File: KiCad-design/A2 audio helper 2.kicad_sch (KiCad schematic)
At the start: 34 parts, among them J1 PIN HEADER 1x2, J10 PIN HEADER 1x2, J11 PIN HEADER 1x3, J12 PIN HEADER 1x3, J13 PIN HEADER 1x3, J2 PIN HEADER 1x2, J3 PIN HEADER 1x2, J4 SJ1-3515N, J5 PIN HEADER 1x3, J6 PIN HEADER 1x3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

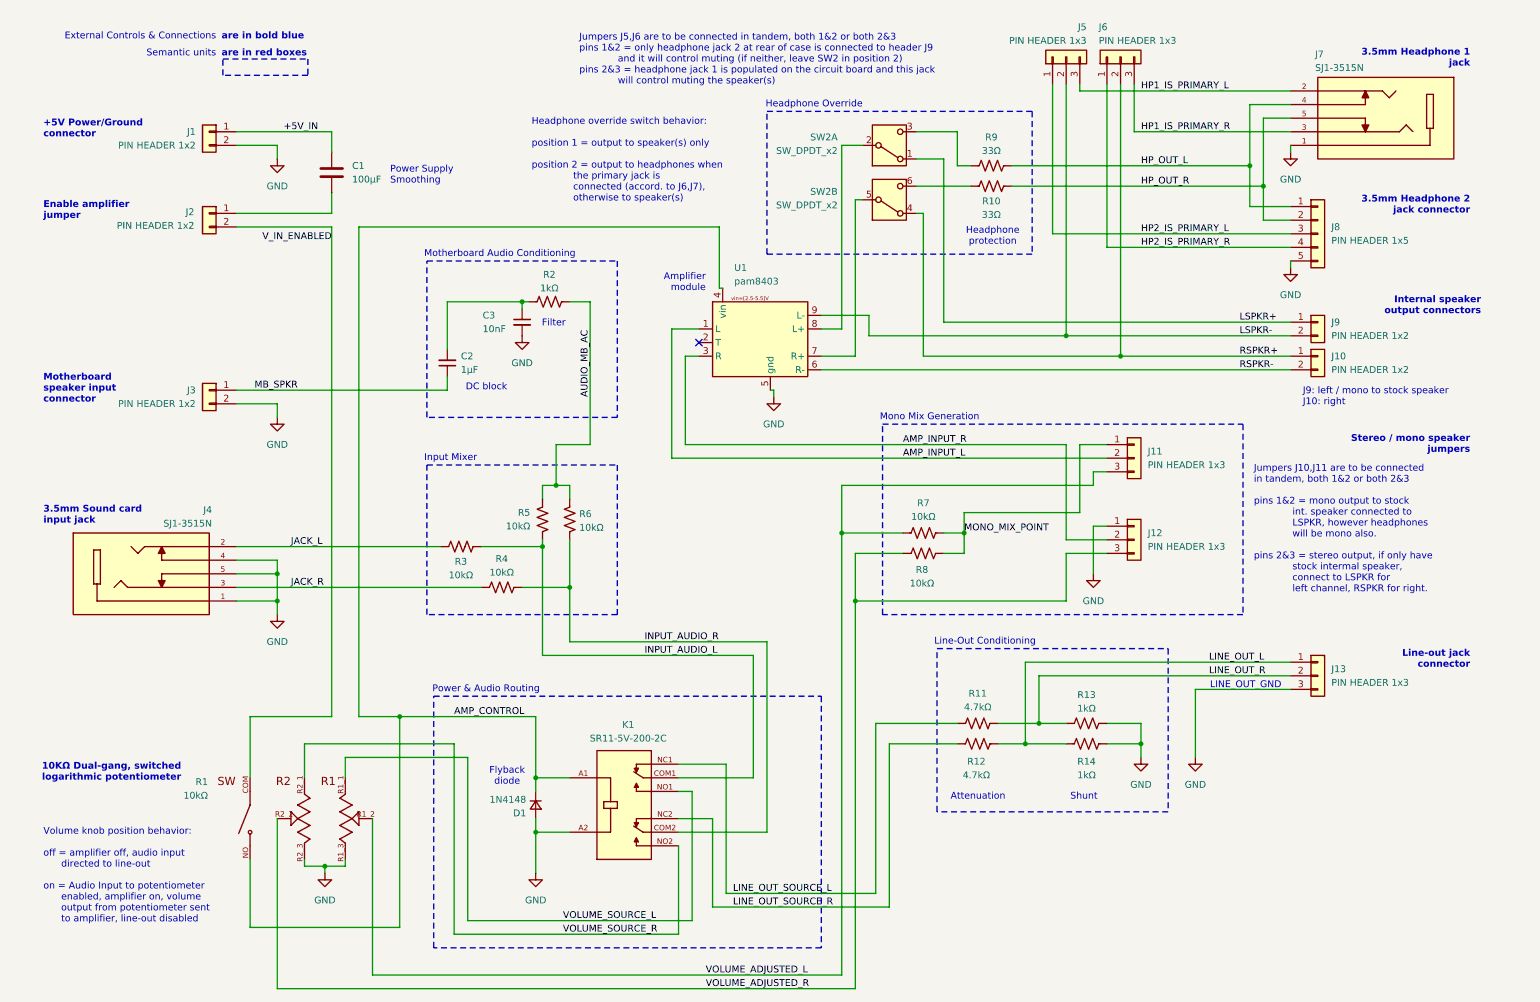
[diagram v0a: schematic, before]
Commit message: ribbon cbl to remote vol & headph board
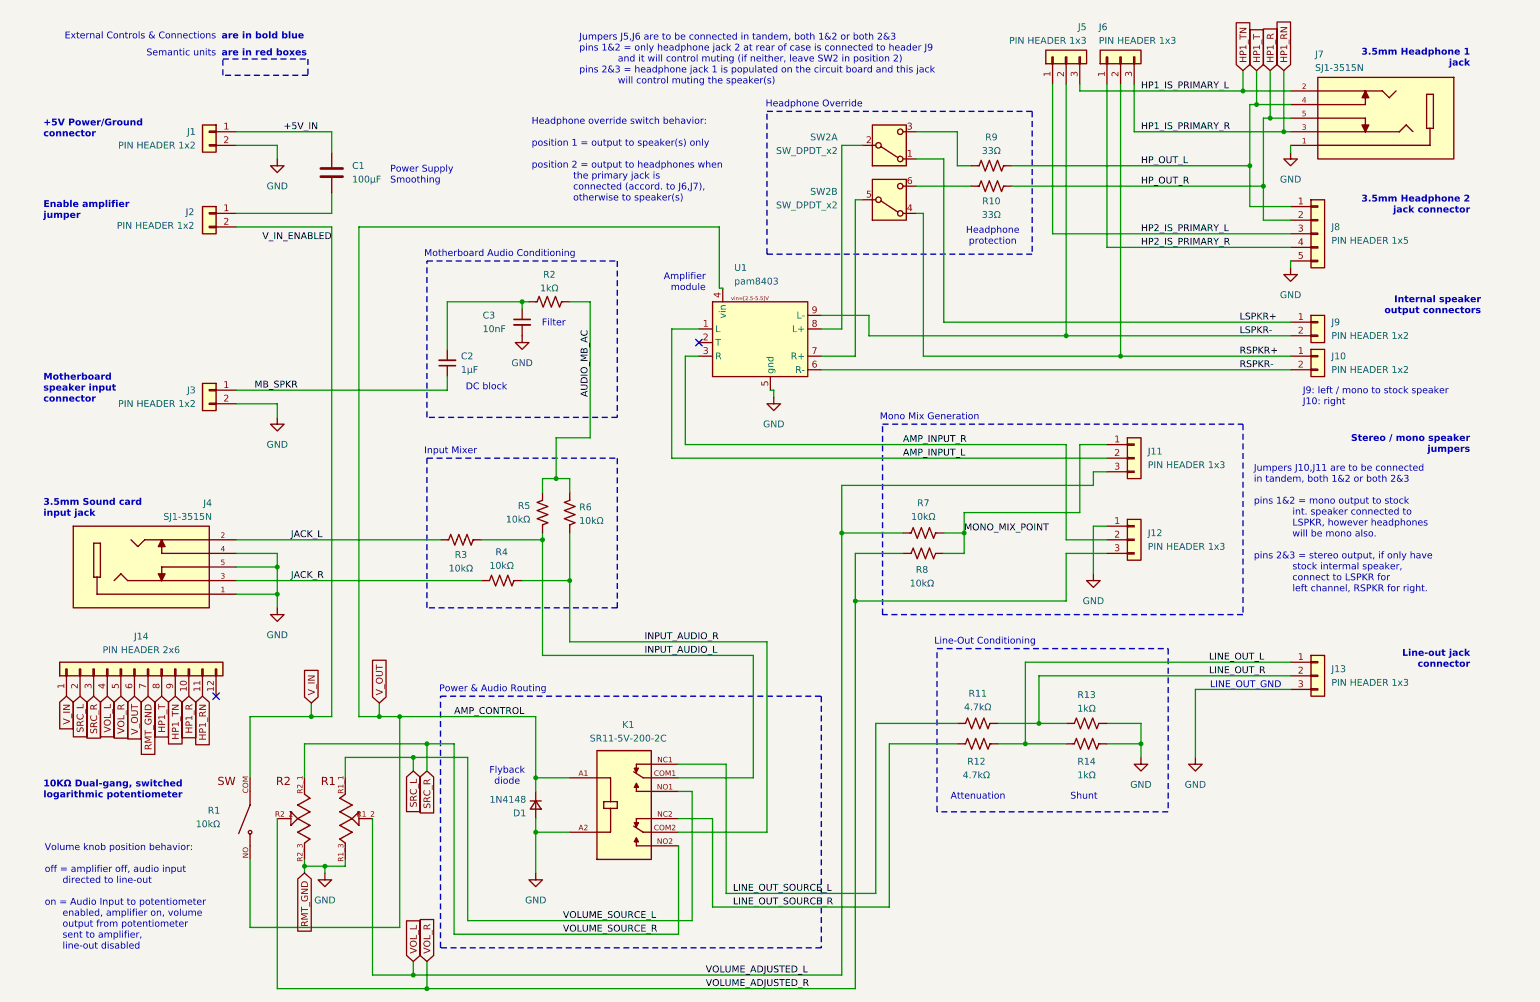
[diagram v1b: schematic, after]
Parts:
- added J14: PIN HEADER 2x6, Connector_PinSocket_2.00mm:PinSocket_2x06_P2.00mm_Vertical, symbol Connector_Generic:Conn_01x12
- J1: footprint footprints:CONN_22035025_MOL -> Molex5267:CONN_22035025_MOL
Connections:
- net GND: now also J14.7 (Pin_7)
- net AMP_CONTROL renamed V_OUT
- net V_OUT: now also J14.6 (Pin_6)
- net HP1_IS_PRIMARY_L renamed HP1_TN
- net HP1_TN: now also J14.9 (Pin_9)
- net HP1_IS_PRIMARY_R renamed HP1_RN
- net HP1_RN: now also J14.11 (Pin_11)
- net HP_OUT_L renamed HP1_T
- net HP1_T: now also J14.8 (Pin_8)
- net HP_OUT_R renamed HP1_R
- net HP1_R: now also J14.10 (Pin_10)
- net VOLUME_ADJUSTED_L renamed VOL_L
- net VOL_L: now also J14.4 (Pin_4)
- net VOLUME_ADJUSTED_R renamed VOL_R
- net VOL_R: now also J14.5 (Pin_5)
- net VOLUME_SOURCE_L renamed SRC_L
- net SRC_L: now also J14.2 (Pin_2)
- net VOLUME_SOURCE_R renamed SRC_R
- net SRC_R: now also J14.3 (Pin_3)
- net V_IN_ENABLED renamed V_IN
- net V_IN: now also J14.1 (Pin_1)
- no-connect marks 1 -> 2
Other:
- moved on the sheet: J4, R3, R4, R5, R6

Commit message: desc'd ribbon conn better in schematic, fixed LSPKR+ error
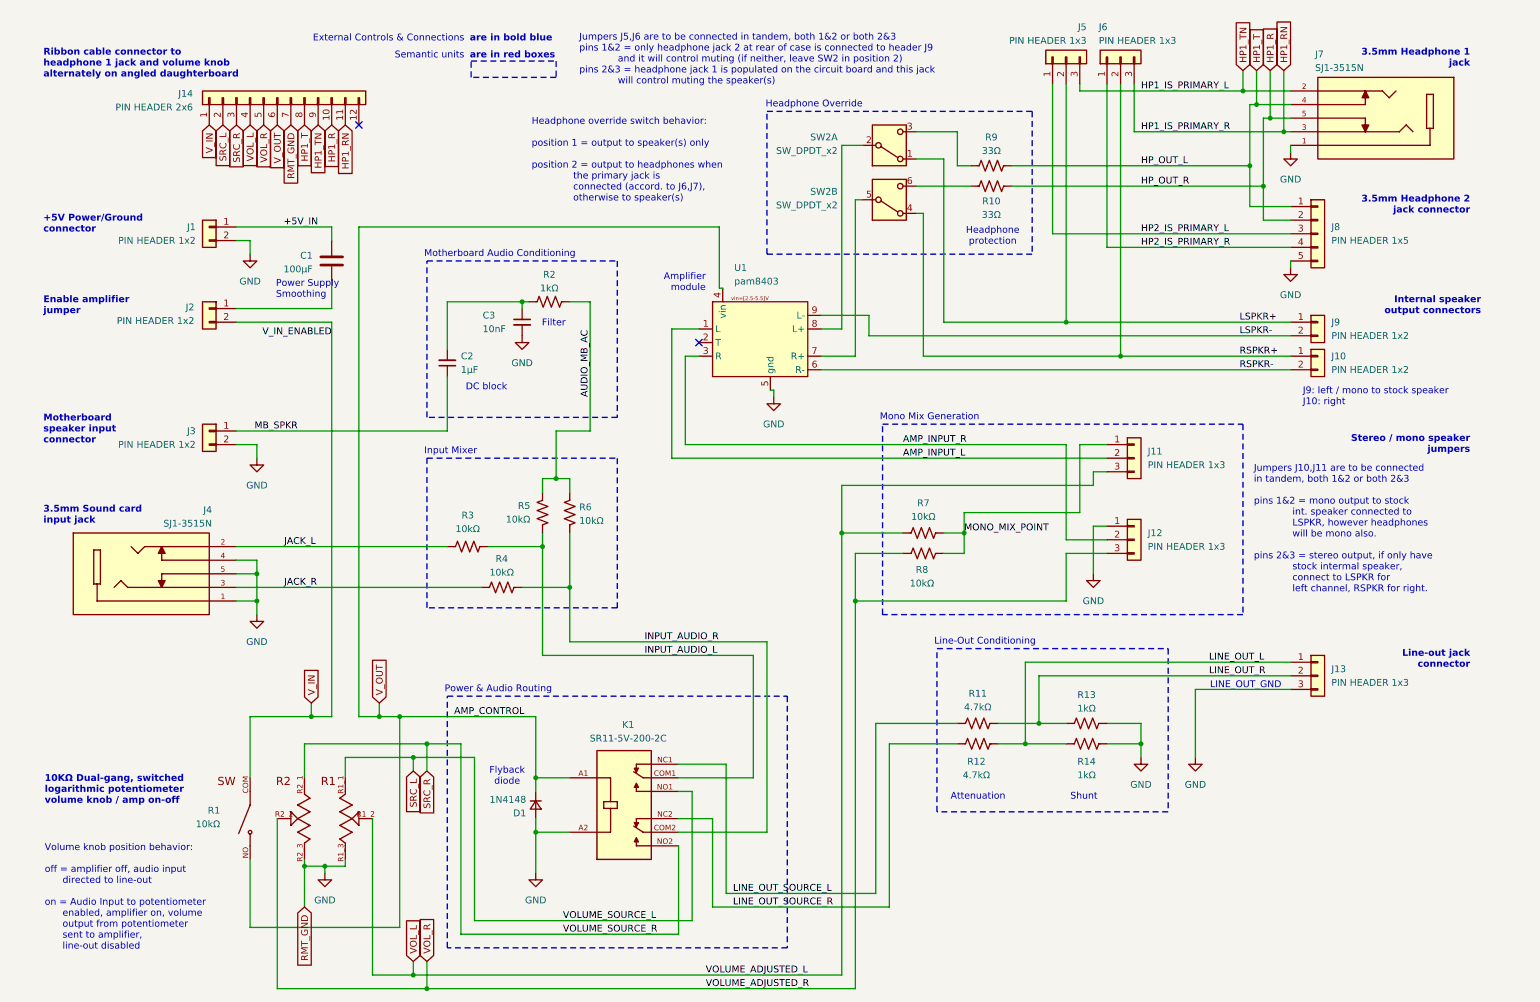
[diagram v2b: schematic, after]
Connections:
- net LSPKR+: now also J5.2 (Pin_2)
- net LSPKR-: no longer J5.2 (Pin_2)
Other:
- note added: "10KΩ Dual-gang, switched logarithmic potentiometer volume knob / amp on-off"
- note added: "Ribbon cable connector to headphone 1 jack and volume knob alternately on angled daughterboard"
- note removed: "10KΩ Dual-gang, switched logarithmic potentiometer"
- moved on the sheet: C1, J1, J14, J2, J3, J4, R3, R4

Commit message: daughtercard pcb, for now connected & perforated
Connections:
- net GND: now also J14.2 (Pin_2); no longer J14.7 (Pin_7)
- net HP1_R: now also J14.7 (Pin_7); no longer J14.10 (Pin_10)
- net HP1_RN: now also J14.8 (Pin_8); no longer J14.11 (Pin_11)
- net HP1_T: now also J14.5 (Pin_5); no longer J14.8 (Pin_8)
- net HP1_TN: now also J14.6 (Pin_6); no longer J14.9 (Pin_9)
- net SRC_L: now also J14.11 (Pin_11); no longer J14.2 (Pin_2)
- net SRC_R: now also J14.9 (Pin_9); no longer J14.3 (Pin_3)
- net VOL_L: now also J14.12 (Pin_12); no longer J14.4 (Pin_4)
- net VOL_R: now also J14.10 (Pin_10); no longer J14.5 (Pin_5)
- net V_OUT: now also J14.3 (Pin_3); no longer J14.6 (Pin_6)
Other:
- added sheet Daughterboard (A2 audio helper 2 daughterboard.kicad_sch)
- moved on the sheet: J14
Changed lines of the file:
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@@
 	(title_block
 		(title "Apple 2 Audio Helper")
-		(date "2026-01-17")
-		(rev "0.7.1")
+		(date "2026-01-24")
+		(rev "0.8")
 		(company "Northwest Retroventures")
 		(comment 1 "Optionally supports second internal speaker for stereo.")
-		(comment 2 "Outputs to line-out jack & headphone jack (rear of case), stock speaker.")
+		(comment 2 "Outputs to line-out jack & headphone jack 2 (rear of case), jack 1 (front), stock speaker.")
 		(comment 3 "Routes sound card and motherboard audio sources. Power from int. game port connector.")
-		(comment 4 "Circuit to mount internal to Apple 2 beneath keyboard, exposing mode & volume knobs.")
+		(comment 4 "Circuit to mount in Apple 2 case beneath keyboard, exposing headph. jack & volume knob.")
 	)
 	(rectangle
@@
 	(text "Ribbon cable connector to\nheadphone 1 jack and volume knob\nalternately on angled daughterboard"
 		(exclude_from_sim no)
-		(at 14.732 21.59 0)
+		(at 14.732 18.288 0)
 		(effects
 			(font
@@
 	)
 	(junction
-		(at 63.5 171.45)
-		(diameter 0)
-		(color 0 0 0 0)
-	)
-	(junction
 		(at 83.82 191.77)
 		(diameter 0)
@@
 	)
 	(no_connect
-		(at 73.66 33.02)
+		(at 53.34 29.21)
 	)
 	(no_connect
@@
 	(wire
 		(pts
+			(xy 48.26 36.83) (xy 43.18 36.83)
+		)
+		(stroke
+			(width 0)
+			(type default)
+		)
+	)
+	(wire
+		(pts
 			(xy 213.36 148.59) (xy 219.71 148.59)
 		)
@@
 	(wire
 		(pts
+			(xy 48.26 29.21) (xy 48.26 36.83)
+		)
+		(stroke
+			(width 0)
+			(type default)
+		)
+	)
+	(wire
+		(pts
 			(xy 90.17 66.04) (xy 90.17 74.93)
 		)
@@
 	(wire
 		(pts
-			(xy 63.5 171.45) (xy 63.5 179.07)
-		)
-		(stroke
-			(width 0)
-			(type default)
-		)
-	)
-	(wire
-		(pts
 			(xy 113.03 119.38) (xy 113.03 129.54)
 		)
@@
 	(global_label "SRC_R"
 		(shape input)
-		(at 50.8 33.02 270)
+		(at 66.04 29.21 270)
 		(fields_autoplaced yes)
 		(effects
@@
 		)
 		(property "Intersheetrefs" "${INTERSHEET_REFS}"
-			(at 50.8 41.9923 90)
-			(effects
-				(font
-					(size 1.27 1.27)
-				)
-				(justify right)
-				(hide yes)
-			)
-		)
-	)
-	(global_label "RMT_GND"
-		(shape input)
-		(at 60.96 33.02 270)
-		(fields_autoplaced yes)
-		(effects
-			(font
-				(size 1.27 1.27)
-			)
-			(justify right)
-		)
-		(property "Intersheetrefs" "${INTERSHEET_REFS}"
-			(at 60.96 44.5323 90)
+			(at 66.04 38.1823 90)
 			(effects
 				(font
@@
 	(global_label "V_IN"
 		(shape input)
-		(at 45.72 33.02 270)
+		(at 45.72 29.21 270)
 		(fields_autoplaced yes)
 		(effects
@@
 		)
 		(property "Intersheetrefs" "${INTERSHEET_REFS}"
-			(at 45.72 39.9967 90)
+			(at 45.72 36.1867 90)
 			(effects
 				(font
@@
 	(global_label "HP1_RN"
 		(shape input)
-		(at 71.12 33.02 270)
+		(at 63.5 29.21 270)
 		(fields_autoplaced yes)
 		(effects
@@
 		)
 		(property "Intersheetrefs" "${INTERSHEET_REFS}"
-			(at 71.12 43.3833 90)
+			(at 63.5 39.5733 90)
 			(effects
 				(font
@@
 	(global_label "VOL_R"
 		(shape input)
-		(at 55.88 33.02 270)
+		(at 68.58 29.21 270)
 		(fields_autoplaced yes)
 		(effects
@@
 		)
 		(property "Intersheetrefs" "${INTERSHEET_REFS}"
-			(at 55.88 41.69 90)
-			(effects
-				(font
-					(size 1.27 1.27)
-				)
-				(justify right)
-				(hide yes)
-			)
-		)
-	)
-	(global_label "RMT_GND"
-		(shape input)
-		(at 63.5 179.07 270)
-		(fields_autoplaced yes)
-		(effects
-			(font
-				(size 1.27 1.27)
-			)
-			(justify right)
-		)
-		(property "Intersheetrefs" "${INTERSHEET_REFS}"
-			(at 63.5 190.5823 90)
+			(at 68.58 37.88 90)
 			(effects
 				(font
@@
 	(global_label "HP1_TN"
 		(shape input)
-		(at 66.04 33.02 270)
+		(at 58.42 29.21 270)
 		(fields_autoplaced yes)
 		(effects
@@
 		)
 		(property "Intersheetrefs" "${INTERSHEET_REFS}"
-			(at 66.04 43.0809 90)
+			(at 58.42 39.2709 90)
 			(effects
 				(font
@@
 	(global_label "V_OUT"
 		(shape input)
-		(at 58.42 33.02 270)
+		(at 50.8 29.21 270)
 		(fields_autoplaced yes)
 		(effects
@@
 		)
 		(property "Intersheetrefs" "${INTERSHEET_REFS}"
-			(at 58.42 41.69 90)
+			(at 50.8 37.88 90)
 			(effects
 				(font
@@
 	(global_label "HP1_T"
 		(shape input)
-		(at 63.5 33.02 270)
+		(at 55.88 29.21 270)
 		(fields_autoplaced yes)
 		(effects
@@
 		)
 		(property "Intersheetrefs" "${INTERSHEET_REFS}"
-			(at 63.5 41.7504 90)
+			(at 55.88 37.9404 90)
 			(effects
 				(font
@@
 	(global_label "VOL_L"
 		(shape input)
-		(at 53.34 33.02 270)
+		(at 73.66 29.21 270)
 		(fields_autoplaced yes)
 		(effects
@@
 		)
 		(property "Intersheetrefs" "${INTERSHEET_REFS}"
-			(at 53.34 41.4481 90)
+			(at 73.66 37.6381 90)
 			(effects
 				(font
@@
 	(global_label "HP1_R"
 		(shape input)
-		(at 68.58 33.02 270)
+		(at 60.96 29.21 270)
 		(fields_autoplaced yes)
 		(effects
@@
 		)
 		(property "Intersheetrefs" "${INTERSHEET_REFS}"
-			(at 68.58 42.0528 90)
+			(at 60.96 38.2428 90)
 			(effects
 				(font
@@
 	(global_label "SRC_L"
 		(shape input)
-		(at 48.26 33.02 270)
+		(at 71.12 29.21 270)
 		(fields_autoplaced yes)
 		(effects
@@
 		)
 		(property "Intersheetrefs" "${INTERSHEET_REFS}"
-			(at 48.26 41.7504 90)
+			(at 71.12 37.9404 90)
 			(effects
 				(font
@@
 	(symbol
 		(lib_id "Connector_Generic:Conn_01x12")
-		(at 58.42 27.94 90)
+		(at 58.42 24.13 90)
 		(unit 1)
 		(exclude_from_sim no)
@@
 		(dnp no)
 		(property "Reference" "J14"
-			(at 42.672 27.178 90)
+			(at 42.672 23.368 90)
 			(effects
 				(font
@@
 		)
 		(property "Value" "PIN HEADER 2x6"
-			(at 42.672 29.718 90)
+			(at 42.672 25.908 90)
 			(effects
 				(font
@@
 		)
 		(property "Footprint" "Connector_PinSocket_2.00mm:PinSocket_2x06_P2.00mm_Vertical"
-			(at 58.42 27.94 0)
+			(at 58.42 24.13 0)
 			(effects
 				(font
@@
 		)
 		(property "Datasheet" "~"
-			(at 58.42 27.94 0)
+			(at 58.42 24.13 0)
 			(effects
 				(font
@@
 		)
 		(property "Description" "Generic connector, single row, 01x12, script generated (kicad-library-utils/schlib/autogen/connector/)"
-			(at 58.42 27.94 0)
+			(at 58.42 24.13 0)
 			(effects
 				(font
@@
 	)
 	(symbol
+		(lib_id "power:GND")
+		(at 43.18 36.83 270)
+		(unit 1)
+		(exclude_from_sim no)
+		(in_bom yes)
+		(on_board yes)
+		(dnp no)
+		(fields_autoplaced yes)
+		(property "Reference" "#PWR016"
+			(at 36.83 36.83 0)
+			(effects
+				(font
+					(size 1.27 1.27)
+				)
+				(hide yes)
+			)
+		)
+		(property "Value" "GND"
+			(at 39.37 36.8299 90)
+			(effects
+				(font
+					(size 1.27 1.27)
+				)
+				(justify right)
+			)
+		)
+		(property "Footprint" ""
+			(at 43.18 36.83 0)
+			(effects
+				(font
+					(size 1.27 1.27)
+				)
+				(hide yes)
+			)
+		)
+		(property "Datasheet" ""
+			(at 43.18 36.83 0)
+			(effects
+				(font
+					(size 1.27 1.27)
+				)
+				(hide yes)
+			)
+		)
+		(property "Description" "Power symbol creates a global label with name \"GND\" , ground"
+			(at 43.18 36.83 0)
+			(effects
+				(font
+					(size 1.27 1.27)
+				)
+				(hide yes)
+			)
+		)
+		(pin "1"
+		)
+		(instances
+			(project ""
+				(path "/5bdcff91-125f-4cf8-8ef8-6f244f2a71f5"
+					(reference "#PWR016")
+					(unit 1)
+				)
+			)
+		)
+	)
+	(symbol
 		(lib_id "Connector_Generic:Conn_01x03")
 		(at 218.44 95.25 0)
@@
 				)
 			)
+		)
+	)
+	(sheet
+		(at 17.78 38.1)
+		(size 13.97 3.81)
+		(exclude_from_sim no)
+		(in_bom yes)
+		(on_board yes)
+		(dnp no)
+		(fields_autoplaced yes)
+		(stroke
+			(width 0.1524)
+			(type solid)
+		)
+		(fill
+			(color 0 0 0 0.0000)
+		)
+		(property "Sheetname" "Daughterboard"
+			(at 17.78 37.3884 0)
+			(effects
+				(font
+					(size 1.27 1.27)
+				)
+				(justify left bottom)
+			)
+		)
+		(property "Sheetfile" "A2 audio helper 2 daughterboard.kicad_sch"
+			(at 17.78 42.4946 0)
+			(effects
+				(font
+					(size 1.27 1.27)
+				)
+				(justify left top)
+			)
+		)
+		(instances
+			(project "A2 audio helper 2"
+				(path "/5bdcff91-125f-4cf8-8ef8-6f244f2a71f5"
+					(page "2")
+				)
+			)
